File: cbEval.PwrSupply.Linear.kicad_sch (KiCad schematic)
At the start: 34 parts, among them J1 CAL.CT3151V1-0, J11 Bergstik-II_6, J12 Header.Hor.2x8.9-103326-0-08, J13 Header.Hor.2x8.9-103326-0-08, J2 CAL.CT3151V1-2, J3 Socket.Hor.2x8.1-5535512-8, J4 Socket.Hor.2x8.1-5535512-8, U1 MIC29151-5.0WU, U2 MIC29151-3.3WU, U3 DS1834AS+

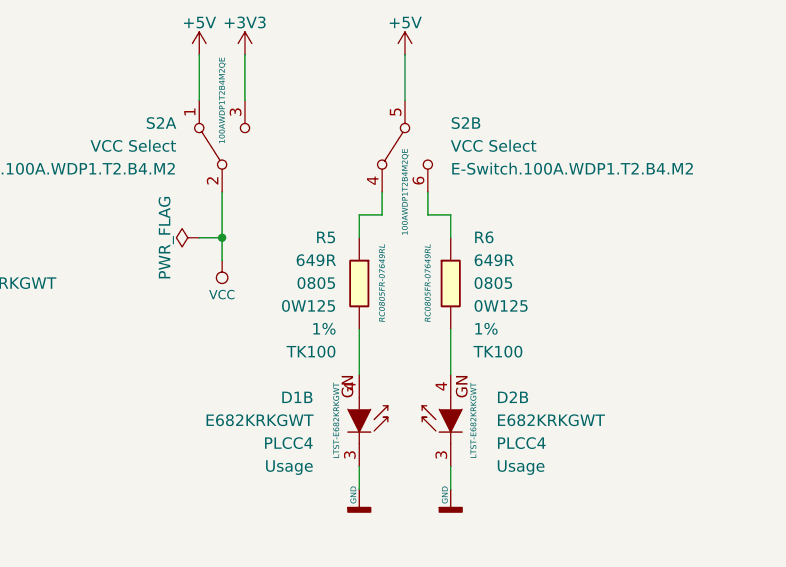
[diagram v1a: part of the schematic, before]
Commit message: Widerstandswerte zur Ansteuerung derngrünen LEDs auf 560 Ohm verringert. Neue Version 1.1.1
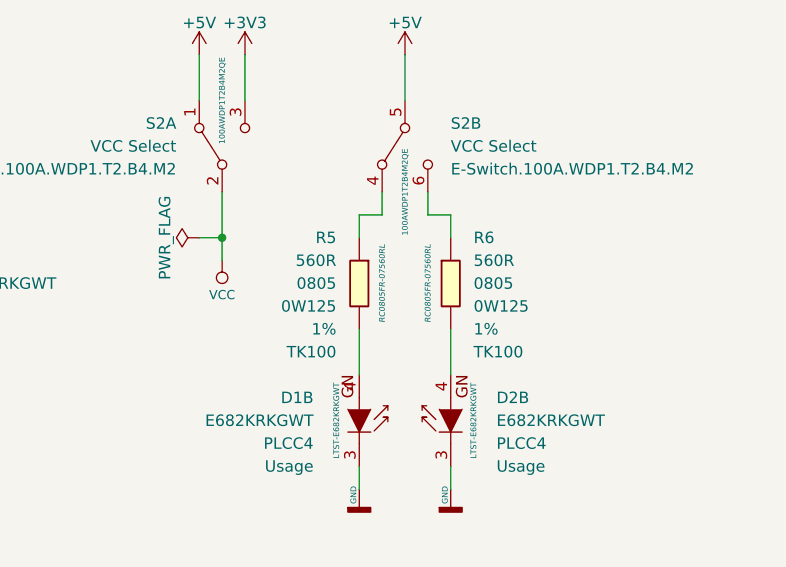
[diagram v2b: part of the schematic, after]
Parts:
- J12, J13: footprint Connector_PinHeader_2.54mm:PinHeader_2x08_P2.54mm_Horizontal -> BTech.PinHeader.2-54mm:PinHeader_2x08_P2.54mm_Horizontal
- R5, R6: value 649R -> 560R; symbol R.Yageo.RC0805:649R -> R.Yageo.RC0805:560R; ID RC0805FR-07649RL -> RC0805FR-07560RL
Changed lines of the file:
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@@
   (title_block
     (title "cbEval PSupply 5P/3P3")
-    (rev "1.1.0")
+    (rev "1.1.1")
   )
   (junction (at 116.84 154.94) (diameter 0.9144) (color 0 0 0 0)
@@
     (property "Reference" "J13" (id 0) (at 109.22 149.86 0))
     (property "Value" "Header.Hor.2x8.9-103326-0-08" (id 1) (at 101.6 170.18 90))
-    (property "Footprint" "Connector_PinHeader_2.54mm:PinHeader_2x08_P2.54mm_Horizontal" (id 2) (at 99.06 170.18 90)
+    (property "Footprint" "BTech.PinHeader.2-54mm:PinHeader_2x08_P2.54mm_Horizontal" (id 2) (at 99.06 170.18 90)
       (effects (font (size 1.016 1.016)) hide)
     )
@@
     (pin "9")
   )
-  (symbol (lib_id "R.Yageo.RC0805:649R") (at 243.84 45.72 0) (mirror y) (unit 1)
+  (symbol (lib_id "R.Yageo.RC0805:560R") (at 243.84 45.72 0) (mirror y) (unit 1)
     (in_bom yes) (on_board yes)
     (property "Reference" "R5" (id 0) (at 241.3 40.64 0)
       (effects (font (size 1.27 1.27)) (justify left))
     )
-    (property "Value" "649R" (id 1) (at 241.3 43.18 0)
+    (property "Value" "560R" (id 1) (at 241.3 43.18 0)
       (effects (font (size 1.27 1.27)) (justify left))
     )
@@
       (effects (font (size 1.27 1.27)) (justify left))
     )
-    (property "ID" "RC0805FR-07649RL" (id 8) (at 246.38 45.72 90)
+    (property "ID" "RC0805FR-07560RL" (id 8) (at 246.38 45.72 90)
       (effects (font (size 0.635 0.635) italic))
     )
@@
     (property "Reference" "J12" (id 0) (at 25.4 149.86 0))
     (property "Value" "Header.Hor.2x8.9-103326-0-08" (id 1) (at 17.78 170.18 90))
-    (property "Footprint" "Connector_PinHeader_2.54mm:PinHeader_2x08_P2.54mm_Horizontal" (id 2) (at 15.24 170.18 90)
+    (property "Footprint" "BTech.PinHeader.2-54mm:PinHeader_2x08_P2.54mm_Horizontal" (id 2) (at 15.24 170.18 90)
       (effects (font (size 1.016 1.016)) hide)
     )
@@
     (pin "1")
   )
-  (symbol (lib_id "R.Yageo.RC0805:649R") (at 254 45.72 0) (unit 1)
+  (symbol (lib_id "R.Yageo.RC0805:560R") (at 254 45.72 0) (unit 1)
     (in_bom yes) (on_board yes)
     (property "Reference" "R6" (id 0) (at 256.54 40.64 0)
       (effects (font (size 1.27 1.27)) (justify left))
     )
-    (property "Value" "649R" (id 1) (at 256.54 43.18 0)
+    (property "Value" "560R" (id 1) (at 256.54 43.18 0)
       (effects (font (size 1.27 1.27)) (justify left))
     )
@@
       (effects (font (size 1.27 1.27)) (justify left))
     )
-    (property "ID" "RC0805FR-07649RL" (id 8) (at 251.46 45.72 90)
+    (property "ID" "RC0805FR-07560RL" (id 8) (at 251.46 45.72 90)
       (effects (font (size 0.635 0.635) italic))
     )
@@
     )
     (path "/ebe28bb3-2b63-4632-ae77-dbef4484ce9f"
-      (reference "J12") (unit 1) (value "Header.Hor.2x8.9-103326-0-08") (footprint "Connector_PinHeader_2.54mm:PinHeader_2x08_P2.54mm_Horizontal")
+      (reference "J12") (unit 1) (value "Header.Hor.2x8.9-103326-0-08") (footprint "BTech.PinHeader.2-54mm:PinHeader_2x08_P2.54mm_Horizontal")
     )
     (path "/27fe4606-788d-4210-80a8-db57dc59cf98"
-      (reference "J13") (unit 1) (value "Header.Hor.2x8.9-103326-0-08") (footprint "Connector_PinHeader_2.54mm:PinHeader_2x08_P2.54mm_Horizontal")
+      (reference "J13") (unit 1) (value "Header.Hor.2x8.9-103326-0-08") (footprint "BTech.PinHeader.2-54mm:PinHeader_2x08_P2.54mm_Horizontal")
     )
     (path "/c9e57e62-be33-4183-8d54-8f35a9c1b2d9"
@@
     )
     (path "/5dd5a9e7-b255-49a9-8213-d4191fc399b1"
-      (reference "R5") (unit 1) (value "649R") (footprint "Resistor_SMD:R_0805_2012Metric")
+      (reference "R5") (unit 1) (value "560R") (footprint "Resistor_SMD:R_0805_2012Metric")
     )
     (path "/f8db61d4-605d-432b-929b-5d27a055bc00"
-      (reference "R6") (unit 1) (value "649R") (footprint "Resistor_SMD:R_0805_2012Metric")
+      (reference "R6") (unit 1) (value "560R") (footprint "Resistor_SMD:R_0805_2012Metric")
     )
     (path "/27513f2c-7924-4132-a700-f6ff7e1f7ca2"
